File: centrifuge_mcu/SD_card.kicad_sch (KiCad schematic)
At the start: 7 parts

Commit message: make and pick footprints for almost everything
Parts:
- C150: renamed from C?; footprint (none) -> Capacitor_SMD:C_0805_2012Metric_Pad1.18x1.45mm_HandSolder; Purchase (none) -> https://www.digikey.no/no/products/detail/taiyo-yuden/LMF21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
- J111: renamed from J?; footprint (none) -> Connector_Card:SD_Kyocera_145638009511859+
- gave numbers to parts that had none: 5
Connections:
- no-connect marks 0 -> 4
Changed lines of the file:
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@@
   (junction (at 139.7 71.12) (diameter 0) (color 0 0 0 0)
   )
+  (no_connect (at 201.295 73.66))
+  (no_connect (at 201.295 71.12))
+  (no_connect (at 201.295 81.28))
+  (no_connect (at 201.295 78.74))
   (wire (pts (xy 147.32 86.36) (xy 149.86 86.36))
     (stroke (width 0) (type default) (color 0 0 0 0))
@@
   (symbol (lib_id "power:GND") (at 140.97 86.36 0) (unit 1)
     (in_bom yes) (on_board yes) (fields_autoplaced)
-    (property "Reference" "#PWR?" (id 0) (at 140.97 92.71 0)
+    (property "Reference" "#PWR0140" (id 0) (at 140.97 92.71 0)
       (effects (font (size 1.27 1.27)) hide)
     )
@@
   (symbol (lib_id "Device:R") (at 139.7 58.42 0) (unit 1)
     (in_bom yes) (on_board yes)
-    (property "Reference" "R?" (id 0) (at 140.97 57.15 0)
+    (property "Reference" "R123" (id 0) (at 138.43 62.23 0)
       (effects (font (size 1.27 1.27)) (justify left))
     )
@@
   (symbol (lib_id "Device:C") (at 147.32 90.17 0) (unit 1)
     (in_bom yes) (on_board yes)
-    (property "Reference" "C?" (id 0) (at 147.955 88.265 0)
+    (property "Reference" "C150" (id 0) (at 147.955 88.265 0)
       (effects (font (size 1.27 1.27)) (justify left))
     )
@@
       (effects (font (size 1.27 1.27)) (justify left))
     )
-    (property "Footprint" "" (id 2) (at 148.2852 93.98 0)
+    (property "Footprint" "Capacitor_SMD:C_0805_2012Metric_Pad1.18x1.45mm_HandSolder" (id 2) (at 148.2852 93.98 0)
       (effects (font (size 1.27 1.27)) hide)
     )
     (property "Datasheet" "~" (id 3) (at 147.32 90.17 0)
+      (effects (font (size 1.27 1.27)) hide)
+    )
+    (property "Purchase" "https://www.digikey.no/no/products/detail/taiyo-yuden/LMF212B7104KGHT/10379109" (id 4) (at 147.32 90.17 0)
       (effects (font (size 1.27 1.27)) hide)
     )
@@
   (symbol (lib_id "Connector:SD_Card") (at 178.435 76.2 0) (unit 1)
     (in_bom yes) (on_board yes) (fields_autoplaced)
-    (property "Reference" "J?" (id 0) (at 178.435 58.42 0))
+    (property "Reference" "J111" (id 0) (at 178.435 58.42 0))
     (property "Value" "SD_Card" (id 1) (at 178.435 60.96 0))
-    (property "Footprint" "" (id 2) (at 178.435 76.2 0)
+    (property "Footprint" "Connector_Card:SD_Kyocera_145638009511859+" (id 2) (at 178.435 76.2 0)
       (effects (font (size 1.27 1.27)) hide)
     )
@@
   (symbol (lib_id "Device:R") (at 144.78 58.42 0) (unit 1)
     (in_bom yes) (on_board yes)
-    (property "Reference" "R?" (id 0) (at 146.05 57.15 0)
+    (property "Reference" "R124" (id 0) (at 143.51 62.23 0)
       (effects (font (size 1.27 1.27)) (justify left))
     )
@@
   (symbol (lib_id "power:+3.3V") (at 129.54 49.53 0) (unit 1)
     (in_bom yes) (on_board yes) (fields_autoplaced)
-    (property "Reference" "#PWR?" (id 0) (at 129.54 53.34 0)
+    (property "Reference" "#PWR0139" (id 0) (at 129.54 53.34 0)
       (effects (font (size 1.27 1.27)) hide)
     )
@@
   (symbol (lib_id "Device:R") (at 134.62 58.42 0) (unit 1)
     (in_bom yes) (on_board yes)
-    (property "Reference" "R?" (id 0) (at 135.89 57.15 0)
+    (property "Reference" "R122" (id 0) (at 133.35 62.23 0)
       (effects (font (size 1.27 1.27)) (justify left))
     )
@@
   (symbol (lib_id "Device:R") (at 149.86 58.42 0) (unit 1)
     (in_bom yes) (on_board yes)
-    (property "Reference" "R?" (id 0) (at 151.13 57.15 0)
+    (property "Reference" "R125" (id 0) (at 148.59 62.23 0)
       (effects (font (size 1.27 1.27)) (justify left))
     )
@@
   (symbol (lib_id "Device:R") (at 155.575 90.17 0) (unit 1)
     (in_bom yes) (on_board yes)
-    (property "Reference" "R?" (id 0) (at 156.845 91.44 0)
-      (effects (font (size 1.27 1.27)) (justify left))
-    )
+    (property "Reference" "R126" (id 0) (at 156.845 91.44 0)
+      (effects (font (size 1.27 1.27)) (justify left))
+    )

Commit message: more footprints, add links to resistor and inductance purchase
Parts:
- R124: renamed from R122; footprint (none) -> Resistor_SMD:R_0805_2012Metric_Pad1.20x1.40mm_HandSolder; Purchase (none) -> https://www.digikey.no/no/products/detail/yageo/AC0805FR-07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
- R125: renamed from R123; footprint (none) -> Resistor_SMD:R_0805_2012Metric_Pad1.20x1.40mm_HandSolder; Purchase (none) -> https://www.digikey.no/no/products/detail/yageo/AC0805FR-07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
- R126: renamed from R124; footprint (none) -> Resistor_SMD:R_0805_2012Metric_Pad1.20x1.40mm_HandSolder; Purchase (none) -> https://www.digikey.no/no/products/detail/yageo/AC0805FR-07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
- R127: renamed from R125; footprint (none) -> Resistor_SMD:R_0805_2012Metric_Pad1.20x1.40mm_HandSolder; Purchase (none) -> https://www.digikey.no/no/products/detail/yageo/AC0805FR-07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
- R128: renamed from R126; footprint (none) -> Resistor_SMD:R_0805_2012Metric_Pad1.20x1.40mm_HandSolder; Purchase (none) -> https://www.digikey.no/no/products/detail/yageo/AC0805FR-07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
- renumbered J111 to J112
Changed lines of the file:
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@@
   (symbol (lib_id "power:GND") (at 140.97 86.36 0) (unit 1)
     (in_bom yes) (on_board yes) (fields_autoplaced)
-    (property "Reference" "#PWR0140" (id 0) (at 140.97 92.71 0)
+    (property "Reference" "#PWR0137" (id 0) (at 140.97 92.71 0)
       (effects (font (size 1.27 1.27)) hide)
     )
@@
   (symbol (lib_id "Device:R") (at 139.7 58.42 0) (unit 1)
     (in_bom yes) (on_board yes)
-    (property "Reference" "R123" (id 0) (at 138.43 62.23 0)
+    (property "Reference" "R125" (id 0) (at 138.43 62.23 0)
       (effects (font (size 1.27 1.27)) (justify left))
     )
@@
       (effects (font (size 1.27 1.27)) (justify left))
     )
-    (property "Footprint" "" (id 2) (at 137.922 58.42 90)
+    (property "Footprint" "Resistor_SMD:R_0805_2012Metric_Pad1.20x1.40mm_HandSolder" (id 2) (at 137.922 58.42 90)
       (effects (font (size 1.27 1.27)) hide)
     )
     (property "Datasheet" "~" (id 3) (at 139.7 58.42 0)
+      (effects (font (size 1.27 1.27)) hide)
+    )
+    (property "Purchase" "https://www.digikey.no/no/products/detail/yageo/AC0805FR-0710KL/2827834" (id 4) (at 139.7 58.42 0)
       (effects (font (size 1.27 1.27)) hide)
     )
@@
   (symbol (lib_id "Connector:SD_Card") (at 178.435 76.2 0) (unit 1)
     (in_bom yes) (on_board yes) (fields_autoplaced)
-    (property "Reference" "J111" (id 0) (at 178.435 58.42 0))
+    (property "Reference" "J112" (id 0) (at 178.435 58.42 0))
     (property "Value" "SD_Card" (id 1) (at 178.435 60.96 0))
     (property "Footprint" "Connector_Card:SD_Kyocera_145638009511859+" (id 2) (at 178.435 76.2 0)
@@
   (symbol (lib_id "Device:R") (at 144.78 58.42 0) (unit 1)
     (in_bom yes) (on_board yes)
-    (property "Reference" "R124" (id 0) (at 143.51 62.23 0)
+    (property "Reference" "R126" (id 0) (at 143.51 62.23 0)
       (effects (font (size 1.27 1.27)) (justify left))
     )
@@
       (effects (font (size 1.27 1.27)) (justify left))
     )
-    (property "Footprint" "" (id 2) (at 143.002 58.42 90)
+    (property "Footprint" "Resistor_SMD:R_0805_2012Metric_Pad1.20x1.40mm_HandSolder" (id 2) (at 143.002 58.42 90)
       (effects (font (size 1.27 1.27)) hide)
     )
     (property "Datasheet" "~" (id 3) (at 144.78 58.42 0)
+      (effects (font (size 1.27 1.27)) hide)
+    )
+    (property "Purchase" "https://www.digikey.no/no/products/detail/yageo/AC0805FR-0710KL/2827834" (id 4) (at 144.78 58.42 0)
       (effects (font (size 1.27 1.27)) hide)
     )
@@
   (symbol (lib_id "power:+3.3V") (at 129.54 49.53 0) (unit 1)
     (in_bom yes) (on_board yes) (fields_autoplaced)
-    (property "Reference" "#PWR0139" (id 0) (at 129.54 53.34 0)
+    (property "Reference" "#PWR0136" (id 0) (at 129.54 53.34 0)
       (effects (font (size 1.27 1.27)) hide)
     )
@@
   (symbol (lib_id "Device:R") (at 134.62 58.42 0) (unit 1)
     (in_bom yes) (on_board yes)
-    (property "Reference" "R122" (id 0) (at 133.35 62.23 0)
+    (property "Reference" "R124" (id 0) (at 133.35 62.23 0)
       (effects (font (size 1.27 1.27)) (justify left))
     )
@@
       (effects (font (size 1.27 1.27)) (justify left))
     )
-    (property "Footprint" "" (id 2) (at 132.842 58.42 90)
+    (property "Footprint" "Resistor_SMD:R_0805_2012Metric_Pad1.20x1.40mm_HandSolder" (id 2) (at 132.842 58.42 90)
       (effects (font (size 1.27 1.27)) hide)
     )
     (property "Datasheet" "~" (id 3) (at 134.62 58.42 0)
+      (effects (font (size 1.27 1.27)) hide)
+    )
+    (property "Purchase" "https://www.digikey.no/no/products/detail/yageo/AC0805FR-0710KL/2827834" (id 4) (at 134.62 58.42 0)
       (effects (font (size 1.27 1.27)) hide)
     )
@@
   (symbol (lib_id "Device:R") (at 149.86 58.42 0) (unit 1)
     (in_bom yes) (on_board yes)
-    (property "Reference" "R125" (id 0) (at 148.59 62.23 0)
+    (property "Reference" "R127" (id 0) (at 148.59 62.23 0)
       (effects (font (size 1.27 1.27)) (justify left))
     )
@@
       (effects (font (size 1.27 1.27)) (justify left))
     )
-    (property "Footprint" "" (id 2) (at 148.082 58.42 90)
+    (property "Footprint" "Resistor_SMD:R_0805_2012Metric_Pad1.20x1.40mm_HandSolder" (id 2) (at 148.082 58.42 90)
       (effects (font (size 1.27 1.27)) hide)
     )
     (property "Datasheet" "~" (id 3) (at 149.86 58.42 0)
+      (effects (font (size 1.27 1.27)) hide)
+    )
+    (property "Purchase" "https://www.digikey.no/no/products/detail/yageo/AC0805FR-0710KL/2827834" (id 4) (at 149.86 58.42 0)
       (effects (font (size 1.27 1.27)) hide)
     )
@@
   (symbol (lib_id "Device:R") (at 155.575 90.17 0) (unit 1)
     (in_bom yes) (on_board yes)
-    (property "Reference" "R126" (id 0) (at 156.845 91.44 0)
+    (property "Reference" "R128" (id 0) (at 156.845 91.44 0)
       (effects (font (size 1.27 1.27)) (justify left))
     )
@@
       (effects (font (size 1.27 1.27)) (justify left))
     )
-    (property "Footprint" "" (id 2) (at 153.797 90.17 90)
+    (property "Footprint" "Resistor_SMD:R_0805_2012Metric_Pad1.20x1.40mm_HandSolder" (id 2) (at 153.797 90.17 90)
       (effects (font (size 1.27 1.27)) hide)
     )
@@
       (effects (font (size 1.27 1.27)) hide)
     )
+    (property "Purchase" "https://www.digikey.no/no/products/detail/yageo/AC0805FR-0710KL/2827834" (id 4) (at 155.575 90.17 0)
+      (effects (font (size 1.27 1.27)) hide)
+    )

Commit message: last footprints, time to route (after final FPGA-board connectors)
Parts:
- renumbered J112 to J114, R124 to R123, R125 to R124, R126 to R125, R127 to R126, R128 to R127
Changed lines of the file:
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@@
   (symbol (lib_id "Device:R") (at 139.7 58.42 0) (unit 1)
     (in_bom yes) (on_board yes)
-    (property "Reference" "R125" (id 0) (at 138.43 62.23 0)
+    (property "Reference" "R124" (id 0) (at 138.43 62.23 0)
       (effects (font (size 1.27 1.27)) (justify left))
     )
@@
   (symbol (lib_id "Connector:SD_Card") (at 178.435 76.2 0) (unit 1)
     (in_bom yes) (on_board yes) (fields_autoplaced)
-    (property "Reference" "J112" (id 0) (at 178.435 58.42 0))
+    (property "Reference" "J114" (id 0) (at 178.435 58.42 0))
     (property "Value" "SD_Card" (id 1) (at 178.435 60.96 0))
     (property "Footprint" "Connector_Card:SD_Kyocera_145638009511859+" (id 2) (at 178.435 76.2 0)
@@
   (symbol (lib_id "Device:R") (at 144.78 58.42 0) (unit 1)
     (in_bom yes) (on_board yes)
-    (property "Reference" "R126" (id 0) (at 143.51 62.23 0)
+    (property "Reference" "R125" (id 0) (at 143.51 62.23 0)
       (effects (font (size 1.27 1.27)) (justify left))
     )
@@
   (symbol (lib_id "Device:R") (at 134.62 58.42 0) (unit 1)
     (in_bom yes) (on_board yes)
-    (property "Reference" "R124" (id 0) (at 133.35 62.23 0)
+    (property "Reference" "R123" (id 0) (at 133.35 62.23 0)
       (effects (font (size 1.27 1.27)) (justify left))
     )
@@
   (symbol (lib_id "Device:R") (at 149.86 58.42 0) (unit 1)
     (in_bom yes) (on_board yes)
-    (property "Reference" "R127" (id 0) (at 148.59 62.23 0)
+    (property "Reference" "R126" (id 0) (at 148.59 62.23 0)
       (effects (font (size 1.27 1.27)) (justify left))
     )
@@
   (symbol (lib_id "Device:R") (at 155.575 90.17 0) (unit 1)
     (in_bom yes) (on_board yes)
-    (property "Reference" "R128" (id 0) (at 156.845 91.44 0)
+    (property "Reference" "R127" (id 0) (at 156.845 91.44 0)
       (effects (font (size 1.27 1.27)) (justify left))
     )

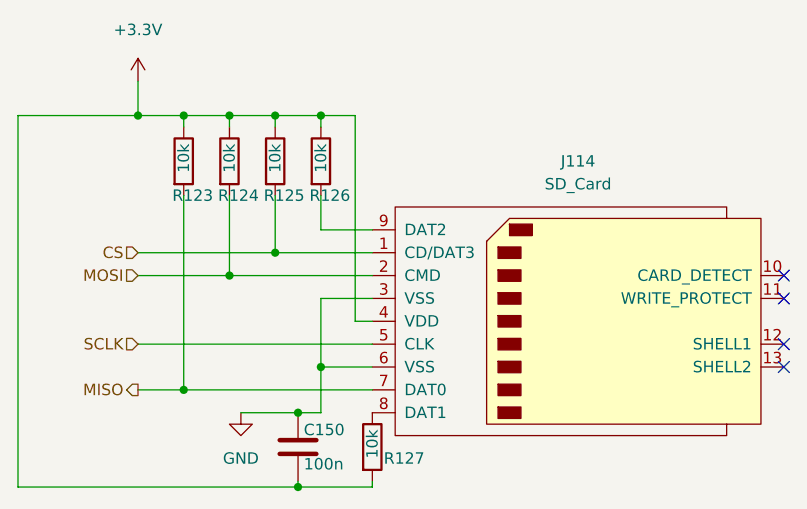
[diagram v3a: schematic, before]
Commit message: start routing PCB for the MCU, starting with power
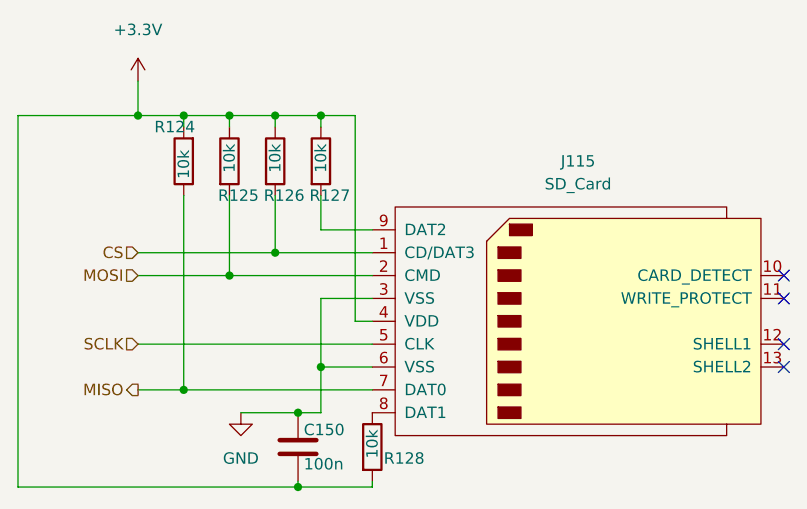
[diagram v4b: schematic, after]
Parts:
- renumbered J114 to J115, R123 to R124, R124 to R125, R125 to R126, R126 to R127, R127 to R128
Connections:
- net +3.3V: now also R124.2; no longer R124.1
- net MISO: now also R124.1; no longer R124.2
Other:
- moved on the sheet: R124
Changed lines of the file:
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@@
   (symbol (lib_id "power:GND") (at 140.97 86.36 0) (unit 1)
     (in_bom yes) (on_board yes) (fields_autoplaced)
-    (property "Reference" "#PWR0137" (id 0) (at 140.97 92.71 0)
+    (property "Reference" "#PWR0139" (id 0) (at 140.97 92.71 0)
       (effects (font (size 1.27 1.27)) hide)
     )
@@
   (symbol (lib_id "Device:R") (at 139.7 58.42 0) (unit 1)
     (in_bom yes) (on_board yes)
-    (property "Reference" "R124" (id 0) (at 138.43 62.23 0)
+    (property "Reference" "R125" (id 0) (at 138.43 62.23 0)
       (effects (font (size 1.27 1.27)) (justify left))
     )
@@
   (symbol (lib_id "Connector:SD_Card") (at 178.435 76.2 0) (unit 1)
     (in_bom yes) (on_board yes) (fields_autoplaced)
-    (property "Reference" "J114" (id 0) (at 178.435 58.42 0))
+    (property "Reference" "J115" (id 0) (at 178.435 58.42 0))
     (property "Value" "SD_Card" (id 1) (at 178.435 60.96 0))
     (property "Footprint" "Connector_Card:SD_Kyocera_145638009511859+" (id 2) (at 178.435 76.2 0)
@@
   (symbol (lib_id "Device:R") (at 144.78 58.42 0) (unit 1)
     (in_bom yes) (on_board yes)
-    (property "Reference" "R125" (id 0) (at 143.51 62.23 0)
+    (property "Reference" "R126" (id 0) (at 143.51 62.23 0)
       (effects (font (size 1.27 1.27)) (justify left))
     )
@@
   (symbol (lib_id "power:+3.3V") (at 129.54 49.53 0) (unit 1)
     (in_bom yes) (on_board yes) (fields_autoplaced)
-    (property "Reference" "#PWR0136" (id 0) (at 129.54 53.34 0)
+    (property "Reference" "#PWR0138" (id 0) (at 129.54 53.34 0)
       (effects (font (size 1.27 1.27)) hide)
     )
@@
     (pin "1")
   )
-  (symbol (lib_id "Device:R") (at 134.62 58.42 0) (unit 1)
+  (symbol (lib_id "Device:R") (at 134.62 58.42 180) (unit 1)
     (in_bom yes) (on_board yes)
-    (property "Reference" "R123" (id 0) (at 133.35 62.23 0)
+    (property "Reference" "R124" (id 0) (at 135.89 54.61 0)
       (effects (font (size 1.27 1.27)) (justify left))
     )
-    (property "Value" "10k" (id 1) (at 134.62 59.69 90)
+    (property "Value" "10k" (id 1) (at 134.62 57.15 90)
       (effects (font (size 1.27 1.27)) (justify left))
     )
-    (property "Footprint" "Resistor_SMD:R_0805_2012Metric_Pad1.20x1.40mm_HandSolder" (id 2) (at 132.842 58.42 90)
+    (property "Footprint" "Resistor_SMD:R_0805_2012Metric_Pad1.20x1.40mm_HandSolder" (id 2) (at 136.398 58.42 90)
       (effects (font (size 1.27 1.27)) hide)
     )
@@
   (symbol (lib_id "Device:R") (at 149.86 58.42 0) (unit 1)
     (in_bom yes) (on_board yes)
-    (property "Reference" "R126" (id 0) (at 148.59 62.23 0)
+    (property "Reference" "R127" (id 0) (at 148.59 62.23 0)
       (effects (font (size 1.27 1.27)) (justify left))
     )
@@
   (symbol (lib_id "Device:R") (at 155.575 90.17 0) (unit 1)
     (in_bom yes) (on_board yes)
-    (property "Reference" "R127" (id 0) (at 156.845 91.44 0)
+    (property "Reference" "R128" (id 0) (at 156.845 91.44 0)
       (effects (font (size 1.27 1.27)) (justify left))
     )

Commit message: continue on power supply routing
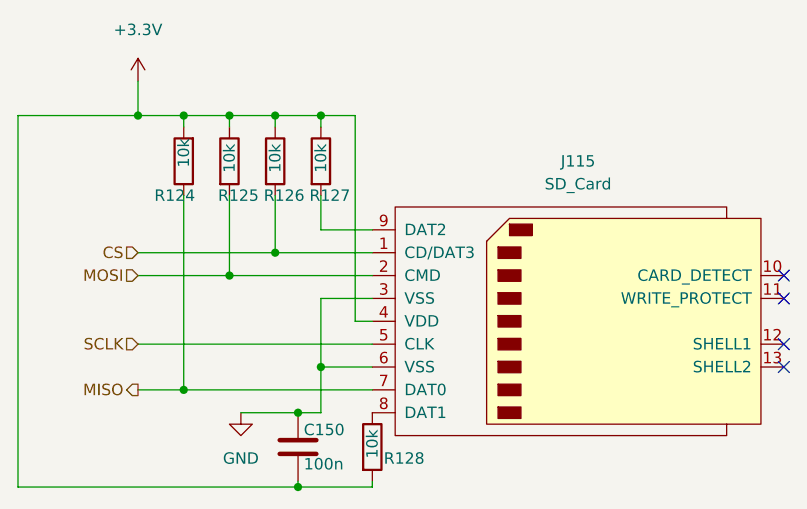
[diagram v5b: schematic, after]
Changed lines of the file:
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@@
   (symbol (lib_id "Device:R") (at 134.62 58.42 180) (unit 1)
     (in_bom yes) (on_board yes)
-    (property "Reference" "R124" (id 0) (at 135.89 54.61 0)
+    (property "Reference" "R124" (id 0) (at 135.89 62.23 0)
       (effects (font (size 1.27 1.27)) (justify left))
     )
-    (property "Value" "10k" (id 1) (at 134.62 57.15 90)
+    (property "Value" "10k" (id 1) (at 134.62 55.88 90)
       (effects (font (size 1.27 1.27)) (justify left))
     )
